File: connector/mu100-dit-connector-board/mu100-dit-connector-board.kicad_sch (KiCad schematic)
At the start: 8 parts, among them J1 Conn_01x17_Male, J2 Conn_01x17, J3 Conn_01x10_Female

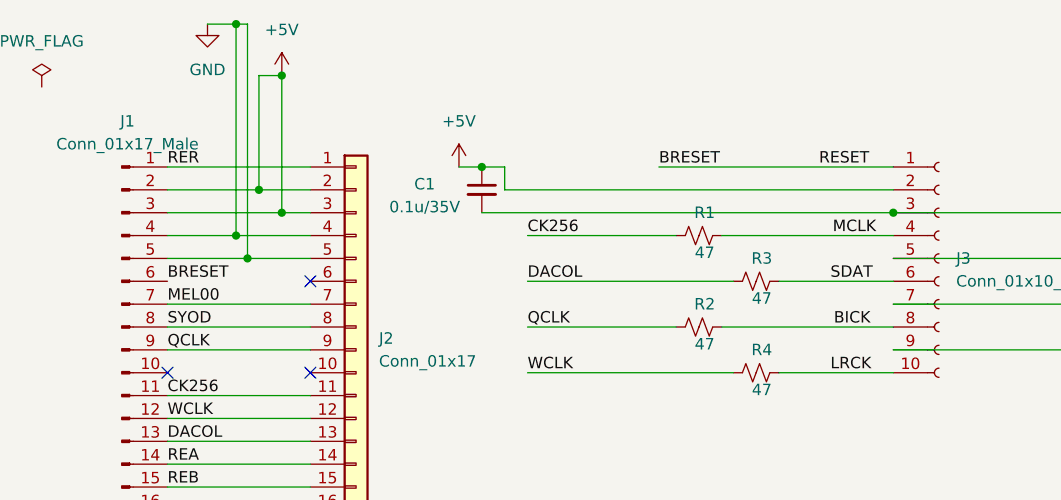
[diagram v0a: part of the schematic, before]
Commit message: Add reset circuit, remove need for reset
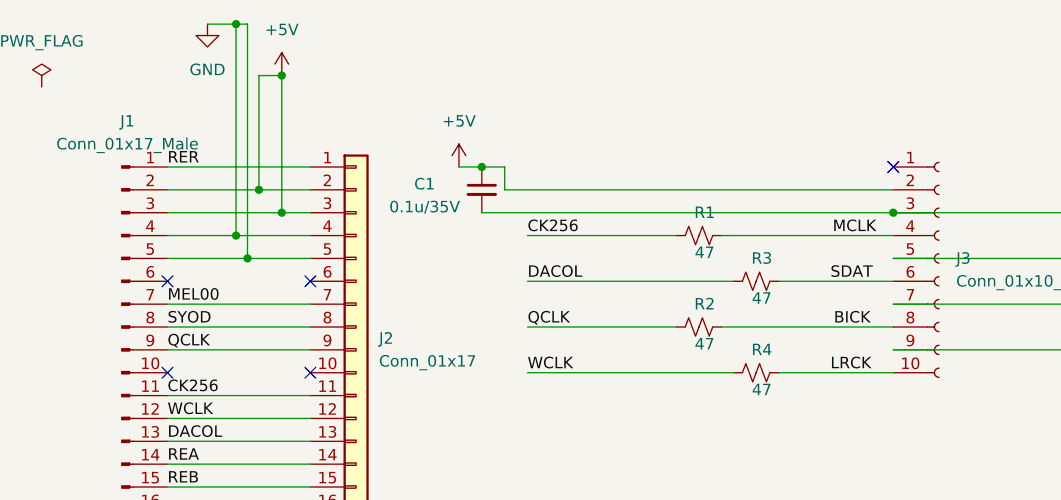
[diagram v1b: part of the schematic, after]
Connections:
- net BRESET: no longer names the net of J3.1 (Pin_1)
- net BRESET: no longer J1.6 (Pin_6)
- no-connect marks 3 -> 5
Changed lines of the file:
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@@
   (junction (at 86.36 104.14) (diameter 0) (color 0 0 0 0)
   )
+  (no_connect (at 156.21 63.5))
+  (no_connect (at 75.565 76.2))
   (no_connect (at 91.44 86.36))
   (no_connect (at 91.44 76.2))
@@
     (stroke (width 0) (type default) (color 0 0 0 0))
   )
-  (wire (pts (xy 130.175 63.5) (xy 156.21 63.5))
-    (stroke (width 0) (type default) (color 0 0 0 0))
-  )
   (wire (pts (xy 113.03 63.5) (xy 110.49 63.5))
     (stroke (width 0) (type default) (color 0 0 0 0))
@@
     (effects (font (size 1.27 1.27)) (justify left bottom))
   )
-  (label "BRESET" (at 130.175 63.5 0)
-    (effects (font (size 1.27 1.27)) (justify left bottom))
-  )
   (label "BICK" (at 153.67 81.28 180)
     (effects (font (size 1.27 1.27)) (justify right bottom))
   )
-  (label "RESET" (at 147.955 63.5 0)
-    (effects (font (size 1.27 1.27)) (justify left bottom))
-  )
-  (label "BRESET" (at 75.565 76.2 0)
-    (effects (font (size 1.27 1.27)) (justify left bottom))
-  )
   (label "SYOD" (at 75.565 81.28 0)

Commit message: finish connector pcb
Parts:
- J2: value Conn_01x17 -> 51247 Molex
- J3: value Conn_01x10_Female -> JST-PH_01x10_Socket
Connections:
- net at J2.10 (Pin_10): now also J1.10 (Pin_10)
- net at J2.6 (Pin_6): now also J1.6 (Pin_6)
- no-connect marks 5 -> 1
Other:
- note added: "+5V"
- note added: "+9VA"
- note added: "100R"
- note added: "47R"
- note added: "AGND"
- note added: "CK256"
- note added: "DACOL"
- note added: "GND"
- note added: "MEL00"
- note added: "MU90R/MU100R wires that went into the Molex connector plug in here"
- note added: "Molex Connector on MU100R/MU90R board -or- unpopulated header on MU100/MU90 board"
- note added: "Note: pins 6 and 10 are actually connected on the MU90 main board, although they are not actually used on the MU90R Analog board"
- note added: "Only MU90R/MU100R has these resistors populated"
- note added: "QCLK"
- note added: "REA"
- note added: "REB"
- note added: "RER"
- note added: "SYOD"
- note added: "WCLK"
- note added: "plugs directly into either the Molex connector or unpopulated header"
- moved on the sheet: C1, J2, J3, R1, R2, R3, R4

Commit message: WIP
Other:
- note added: "Note: pins 6 and 10 are actually connected on the MU90 main board, although they are not actually connected on the MU90R Analog board"
- note removed: "Note: pins 6 and 10 are actually connected on the MU90 main board, although they are not actually used on the MU90R Analog board"
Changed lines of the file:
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@@
+    (stroke (width 0) (type default) (color 0 0 0 0))
+  )
+  (polyline (pts (xy 30.48 86.36) (xy 71.12 86.36))
     (stroke (width 0) (type default) (color 0 0 0 0))
   )
@@
   )
   (polyline (pts (xy 38.735 99.695) (xy 38.735 99.06))
+    (stroke (width 0) (type default) (color 0 0 0 0))
+  )
+  (polyline (pts (xy 30.48 76.2) (xy 71.12 76.2))
     (stroke (width 0) (type default) (color 0 0 0 0))
   )
@@
     (effects (font (size 1.27 1.27)) (justify left bottom))
   )
-  (text "Note: pins 6 and 10 are actually connected on the MU90 \nmain board, although they are not actually used on the MU90R \nAnalog board"
+  (text "Note: pins 6 and 10 are actually connected on the MU90 \nmain board, although they are not actually connected on the MU90R \nAnalog board"
     (at 67.945 41.275 0)
     (effects (font (size 1.27 1.27)) (justify left bottom))
